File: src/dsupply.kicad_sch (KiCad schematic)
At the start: 74 parts, among them J8 Barrel_Jack, Q3 AOSP21321, Q4 AOSP21321, Q5 AOSP21321, Q6 BC857, Q7 BC857, Q8 BC857, Q9 BC857, U24 SDAPO PM1202, U25 AMS1117-3.3, U26 TPS54620

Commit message: sch: correct MFR/PNs for BSS138, TLV9001, TPS54620
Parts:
- U26: MFR_PN TPS54620RHLR -> TPS54620RGYR
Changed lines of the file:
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@@
       (effects (font (size 1.27 1.27)) hide)
     )
-    (property "MFR_PN" "TPS54620RHLR" (at 157.48 160.02 0)
+    (property "MFR_PN" "TPS54620RGYR" (at 157.48 160.02 0)
       (effects (font (size 1.27 1.27)) hide)
     )

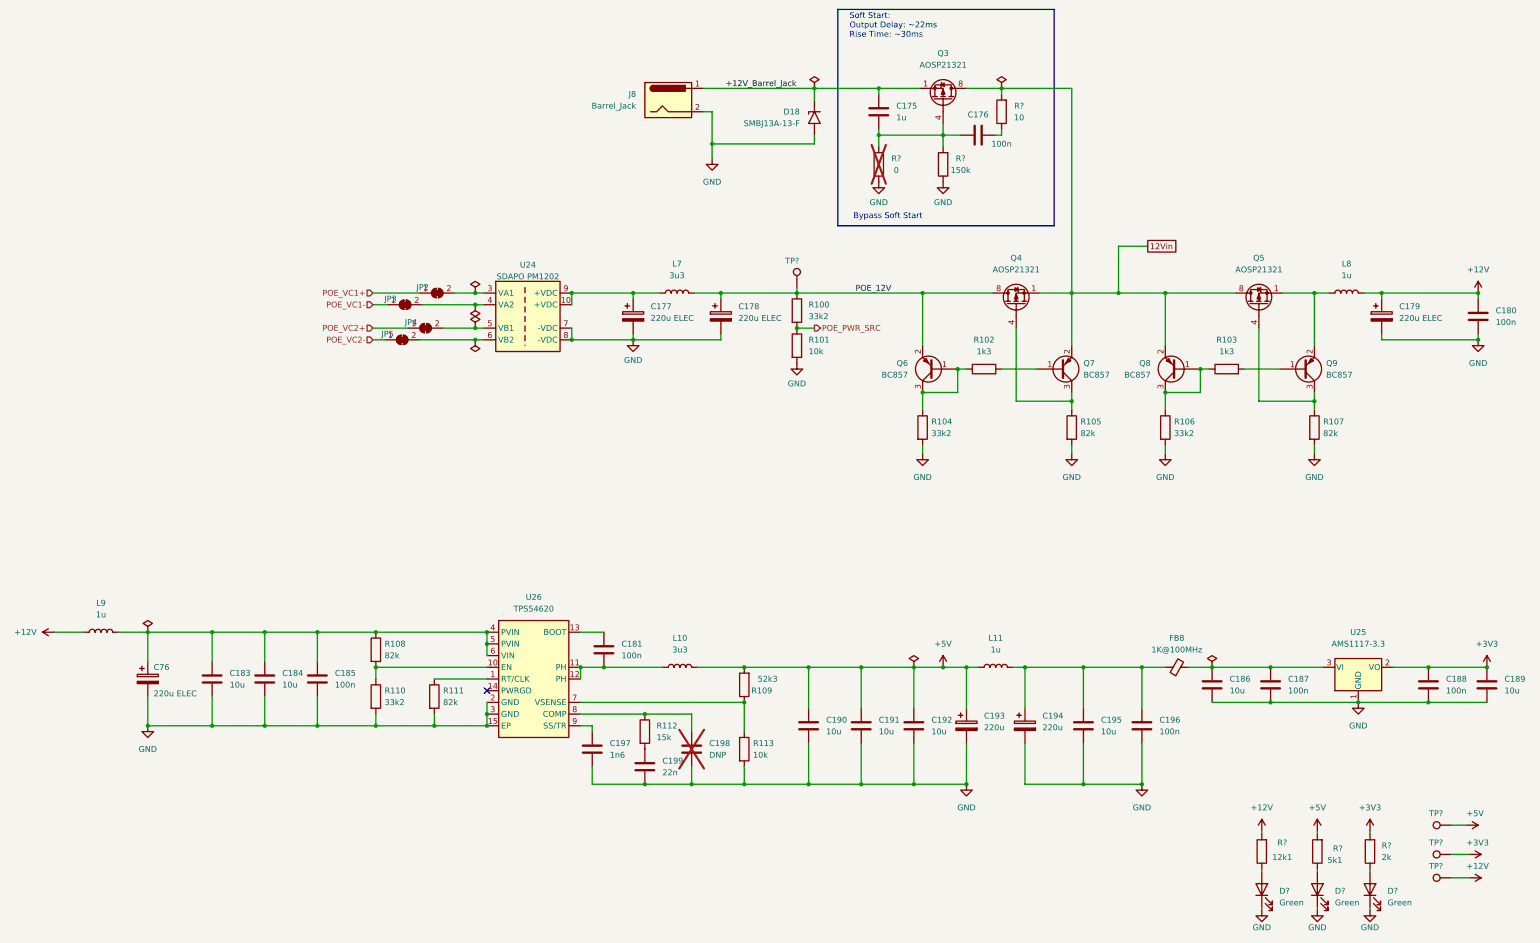
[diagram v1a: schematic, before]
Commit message: Fix issiues from lis, see bug/issiue list in DOC directory
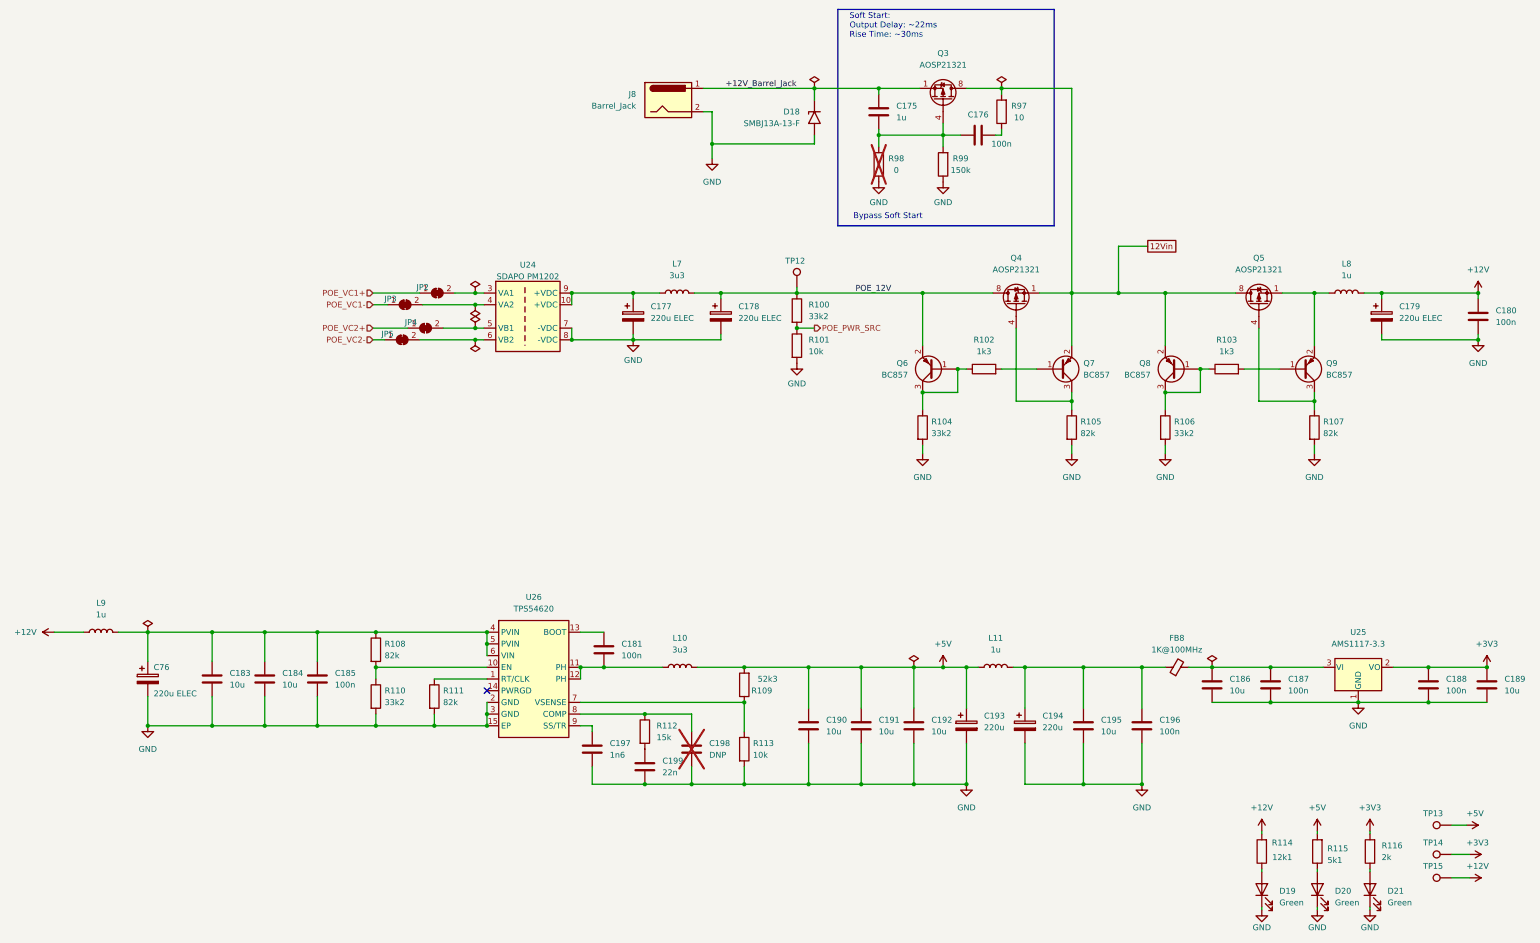
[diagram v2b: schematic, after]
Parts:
- gave numbers to parts that had none: 13
